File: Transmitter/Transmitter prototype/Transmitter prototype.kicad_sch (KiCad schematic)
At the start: 15 parts, among them J1 Conn_Coaxial, J2 Conn_01x03, J3 Conn_01x02, J4 Conn_01x02_Socket, U1 OPA3692IDBQT

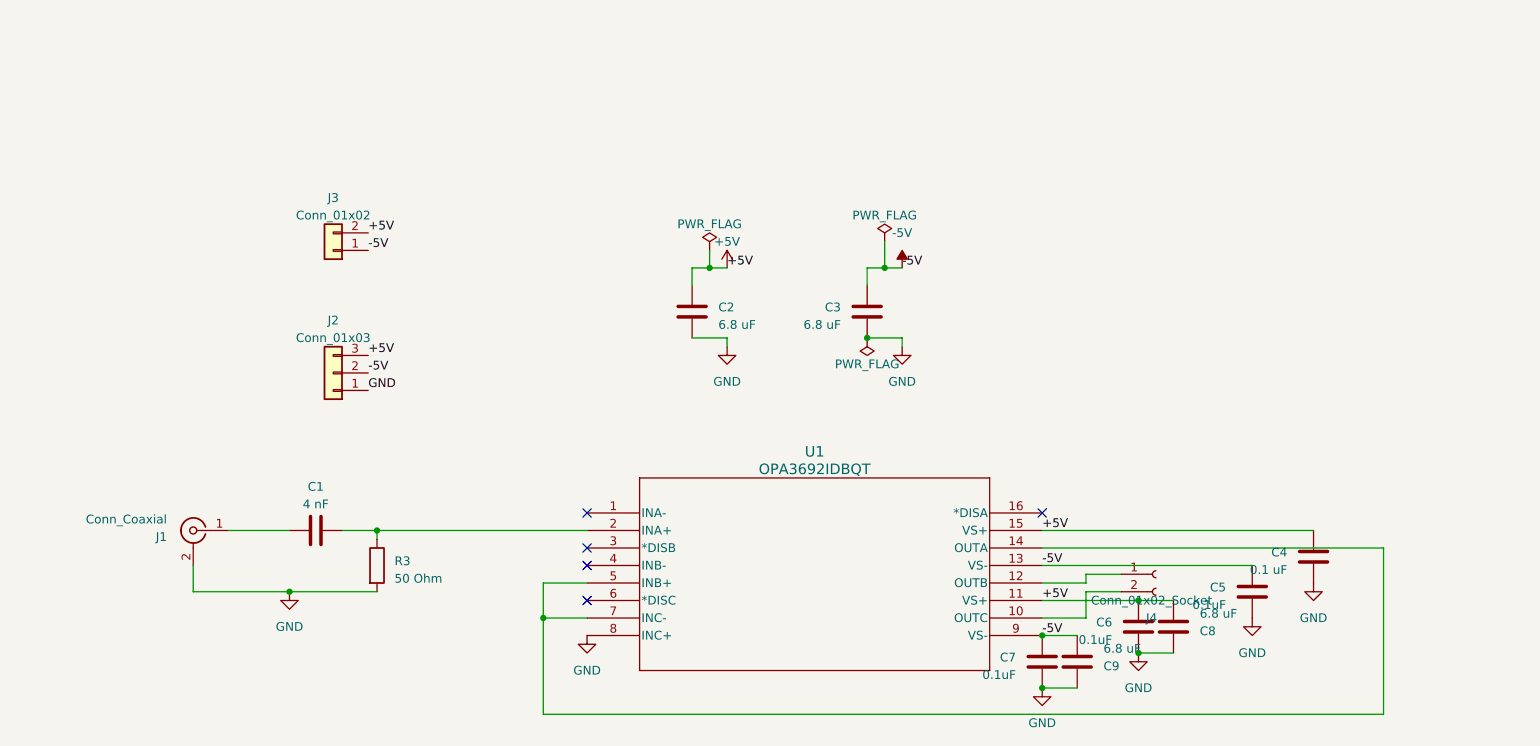
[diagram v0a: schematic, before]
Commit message: Changed coax footprint for TX added pinheaders for test points for out A and coil start / end
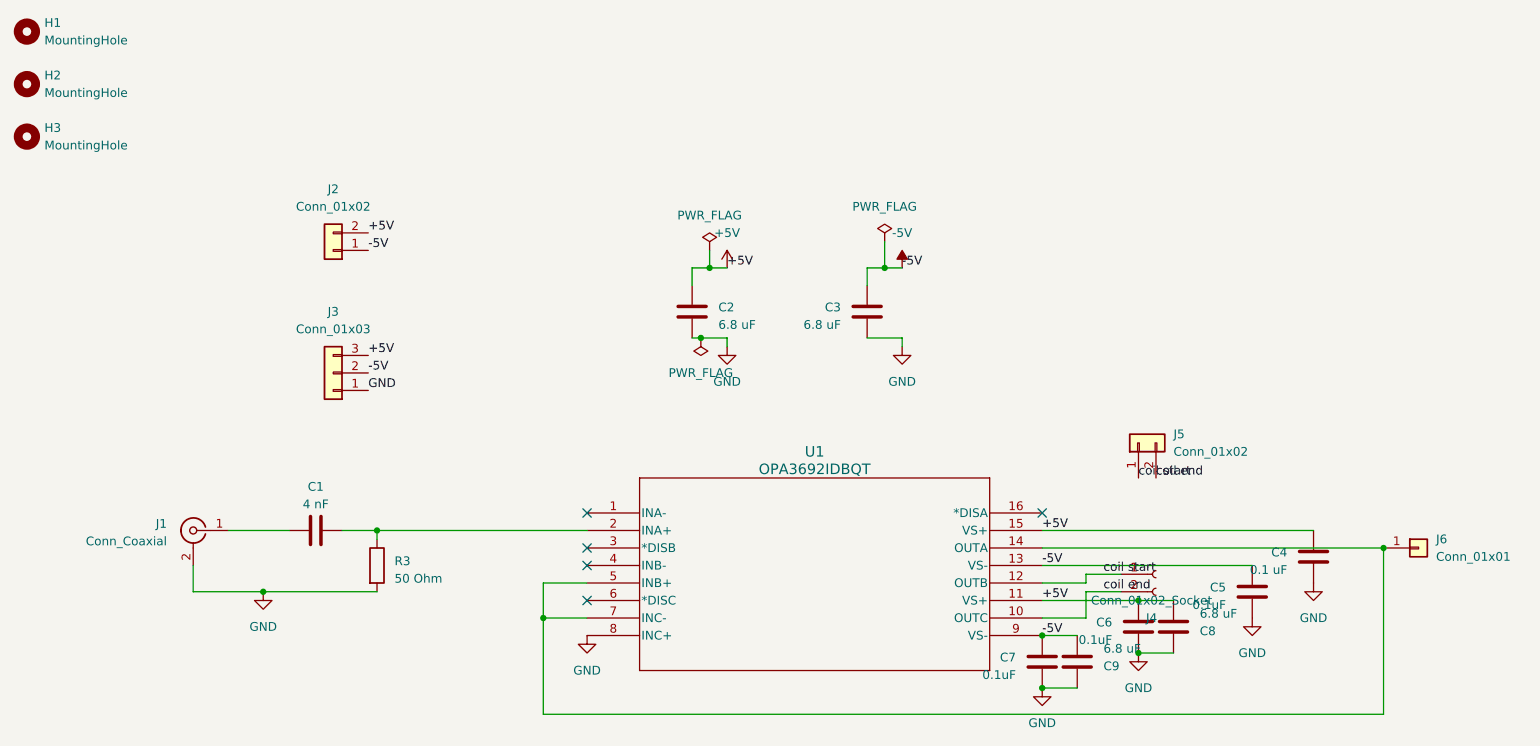
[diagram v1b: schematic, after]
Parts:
- removed J2: Conn_01x03, Connector_PinHeader_2.54mm:PinHeader_1x03_P2.54mm_Vertical, symbol Connector_Generic:Conn_01x03
- removed J3: Conn_01x02, Connector_PinHeader_2.54mm:PinHeader_1x02_P2.54mm_Vertical, symbol Connector_Generic:Conn_01x02
- added H1, H2, H3: MountingHole, MountingHole:MountingHole_2.5mm_Pad, symbol Mechanical:MountingHole
- added J2, J5: Conn_01x02, Connector_PinHeader_2.54mm:PinHeader_1x02_P2.54mm_Vertical, symbol Connector_Generic:Conn_01x02
- added J3: Conn_01x03, Connector_PinHeader_2.54mm:PinHeader_1x03_P2.54mm_Vertical, symbol Connector_Generic:Conn_01x03
- added J6: Conn_01x01, Connector_PinHeader_2.54mm:PinHeader_1x01_P2.54mm_Vertical, symbol Connector_Generic:Conn_01x01
- J1: footprint Connector_Coaxial:BNC_TEConnectivity_1478204_Vertical -> Amphenol 112404:CONN_112404_AMP
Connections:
- net +5V: now also J2.2 (Pin_2), J3.3 (Pin_3)
- net -5V: now also J2.1 (Pin_1), J3.2 (Pin_2)
- net GND: now also J3.1 (Pin_1)
- net coil start: now reaches J4.1 (Pin_1), U1.12 (OUTB)
- net coil start: now also J5.1 (Pin_1)
- net coil end: now reaches J4.2 (Pin_2), U1.10 (OUTC)
- net coil end: now also J5.2 (Pin_2)
- net at U1.14 (OUTA), U1.5 (INB+), U1.7 (INC-): now also J6.1 (Pin_1)

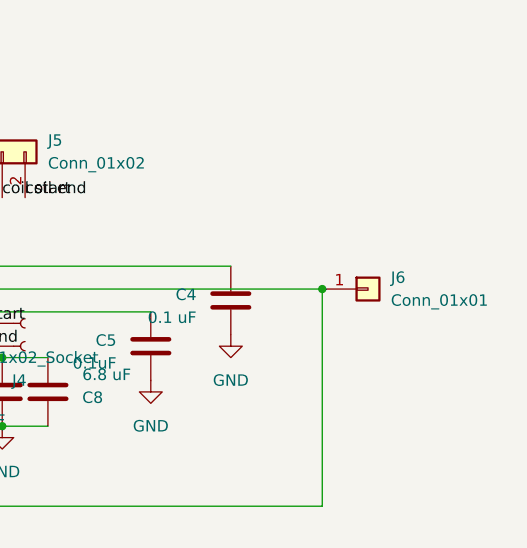
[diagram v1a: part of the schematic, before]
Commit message: added footprints for SOIC and SSOP for OPA3692
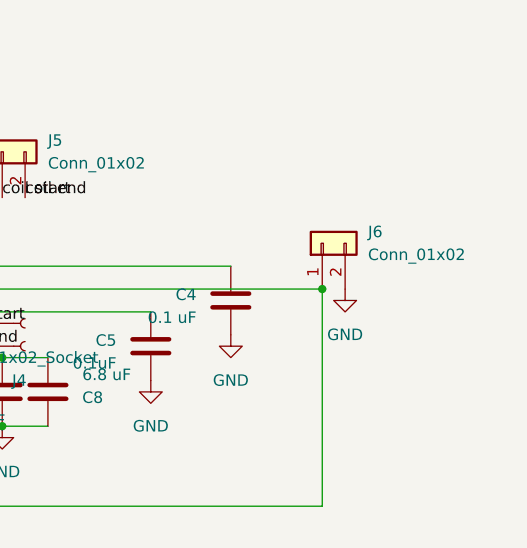
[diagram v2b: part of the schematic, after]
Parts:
- removed J6: Conn_01x01, Connector_PinHeader_2.54mm:PinHeader_1x01_P2.54mm_Vertical, symbol Connector_Generic:Conn_01x01
- added J6: Conn_01x02, Connector_PinHeader_2.54mm:PinHeader_1x02_P2.54mm_Vertical, symbol Connector_Generic:Conn_01x02
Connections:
- net GND: now also J6.2 (Pin_2)
- net at U1.14 (OUTA), U1.5 (INB+), U1.7 (INC-): now also J6.1 (Pin_1)
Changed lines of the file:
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@@
 	(paper "A4")
+	(junction
+		(at 181.61 105.41)
+		(diameter 0)
+		(color 0 0 0 0)
+	)
+	(junction
+		(at 119.38 57.15)
+		(diameter 0)
+		(color 0 0 0 0)
+	)
+	(junction
+		(at 71.12 95.25)
+		(diameter 0)
+		(color 0 0 0 0)
+	)
+	(junction
+		(at 167.64 110.49)
+		(diameter 0)
+		(color 0 0 0 0)
+	)
+	(junction
+		(at 118.11 67.31)
+		(diameter 0)
+		(color 0 0 0 0)
+	)
+	(junction
+		(at 144.78 57.15)
+		(diameter 0)
+		(color 0 0 0 0)
+	)
 	(junction
 		(at 217.17 97.79)
@@
 	)
 	(junction
-		(at 181.61 105.41)
-		(diameter 0)
-		(color 0 0 0 0)
-	)
-	(junction
-		(at 119.38 57.15)
-		(diameter 0)
-		(color 0 0 0 0)
-	)
-	(junction
-		(at 71.12 95.25)
-		(diameter 0)
-		(color 0 0 0 0)
-	)
-	(junction
-		(at 167.64 110.49)
-		(diameter 0)
-		(color 0 0 0 0)
-	)
-	(junction
-		(at 118.11 67.31)
-		(diameter 0)
-		(color 0 0 0 0)
-	)
-	(junction
-		(at 144.78 57.15)
-		(diameter 0)
-		(color 0 0 0 0)
-	)
-	(junction
 		(at 54.61 104.14)
 		(diameter 0)
@@
 	)
 	(symbol
-		(lib_id "Connector_Generic:Conn_01x01")
-		(at 222.25 97.79 0)
-		(unit 1)
-		(exclude_from_sim no)
-		(in_bom yes)
-		(on_board yes)
-		(dnp no)
-		(fields_autoplaced yes)
-		(property "Reference" "J6"
-			(at 224.79 96.5199 0)
-			(effects
-				(font
-					(size 1.27 1.27)
-				)
-				(justify left)
-			)
-		)
-		(property "Value" "Conn_01x01"
-			(at 224.79 99.0599 0)
-			(effects
-				(font
-					(size 1.27 1.27)
-				)
-				(justify left)
-			)
-		)
-		(property "Footprint" "Connector_PinHeader_2.54mm:PinHeader_1x01_P2.54mm_Vertical"
-			(at 222.25 97.79 0)
-			(effects
-				(font
-					(size 1.27 1.27)
-				)
-				(hide yes)
-			)
-		)
-		(property "Datasheet" "~"
-			(at 222.25 97.79 0)
-			(effects
-				(font
-					(size 1.27 1.27)
-				)
-				(hide yes)
-			)
-		)
-		(property "Description" "Generic connector, single row, 01x01, script generated (kicad-library-utils/schlib/autogen/connector/)"
-			(at 222.25 97.79 0)
-			(effects
-				(font
-					(size 1.27 1.27)
-				)
-				(hide yes)
-			)
-		)
-		(pin "1"
-		)
-		(instances
-			(project "Transmitter prototype"
-				(path "/c11cda7e-a7f0-42b6-b4a5-7aa6ec037d29"
-					(reference "J6")
-					(unit 1)
-				)
-			)
-		)
-	)
-	(symbol
 		(lib_id "Device:C")
 		(at 167.64 114.3 0)
@@
 				(path "/c11cda7e-a7f0-42b6-b4a5-7aa6ec037d29"
 					(reference "#PWR07")
+					(unit 1)
+				)
+			)
+		)
+	)
+	(symbol
+		(lib_id "Connector_Generic:Conn_01x02")
+		(at 217.17 92.71 90)
+		(unit 1)
+		(exclude_from_sim no)
+		(in_bom yes)
+		(on_board yes)
+		(dnp no)
+		(fields_autoplaced yes)
+		(property "Reference" "J6"
+			(at 222.25 91.4399 90)
+			(effects
+				(font
+					(size 1.27 1.27)
+				)
+				(justify right)
+			)
+		)
+		(property "Value" "Conn_01x02"
+			(at 222.25 93.9799 90)
+			(effects
+				(font
+					(size 1.27 1.27)
+				)
+				(justify right)
+			)
+		)
+		(property "Footprint" "Connector_PinHeader_2.54mm:PinHeader_1x02_P2.54mm_Vertical"
+			(at 217.17 92.71 0)
+			(effects
+				(font
+					(size 1.27 1.27)
+				)
+				(hide yes)
+			)
+		)
+		(property "Datasheet" "~"
+			(at 217.17 92.71 0)
+			(effects
+				(font
+					(size 1.27 1.27)
+				)
+				(hide yes)
+			)
+		)
+		(property "Description" "Generic connector, single row, 01x02, script generated (kicad-library-utils/schlib/autogen/connector/)"
+			(at 217.17 92.71 0)
+			(effects
+				(font
+					(size 1.27 1.27)
+				)
+				(hide yes)
+			)
+		)
+		(pin "2"
+		)
+		(pin "1"
+		)
+		(instances
+			(project "Transmitter prototype"
+				(path "/c11cda7e-a7f0-42b6-b4a5-7aa6ec037d29"
+					(reference "J6")
 					(unit 1)
 				)
@@
 					(unit 1)
 				)
+			)
+		)
+	)
+	(symbol
+		(lib_name "GND_1")
+		(lib_id "power:GND")
+		(at 219.71 97.79 0)
+		(unit 1)
+		(exclude_from_sim no)
+		(in_bom yes)
+		(on_board yes)
+		(dnp no)
+		(fields_autoplaced yes)
+		(property "Reference" "#PWR010"
+			(at 219.71 104.14 0)
+			(effects
+				(font
+					(size 1.27 1.27)
+				)
+				(hide yes)
+			)
+		)
+		(property "Value" "GND"
+			(at 219.71 102.87 0)
+			(effects
+				(font
+					(size 1.27 1.27)
+				)
+			)
+		)
+		(property "Footprint" ""
+			(at 219.71 97.79 0)
+			(effects
+				(font
+					(size 1.27 1.27)
+				)
+				(hide yes)
+			)
+		)
+		(property "Datasheet" ""
+			(at 219.71 97.79 0)
+			(effects
+				(font
+					(size 1.27 1.27)
+				)
+				(hide yes)
+			)
+		)
+		(property "Description" "Power symbol creates a global label with name \"GND\" , ground"
+			(at 219.71 97.79 0)
+			(effects
+				(font
+					(size 1.27 1.27)
+				)
+				(hide yes)
+			)
+		)
+		(pin "1"
+		)
+		(instances
+			(project "Transmitter prototype"
+				(path "/c11cda7e-a7f0-42b6-b4a5-7aa6ec037d29"
+					(reference "#PWR010")
+					(unit 1)
+				)
